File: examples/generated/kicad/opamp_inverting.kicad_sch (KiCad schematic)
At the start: 6 parts

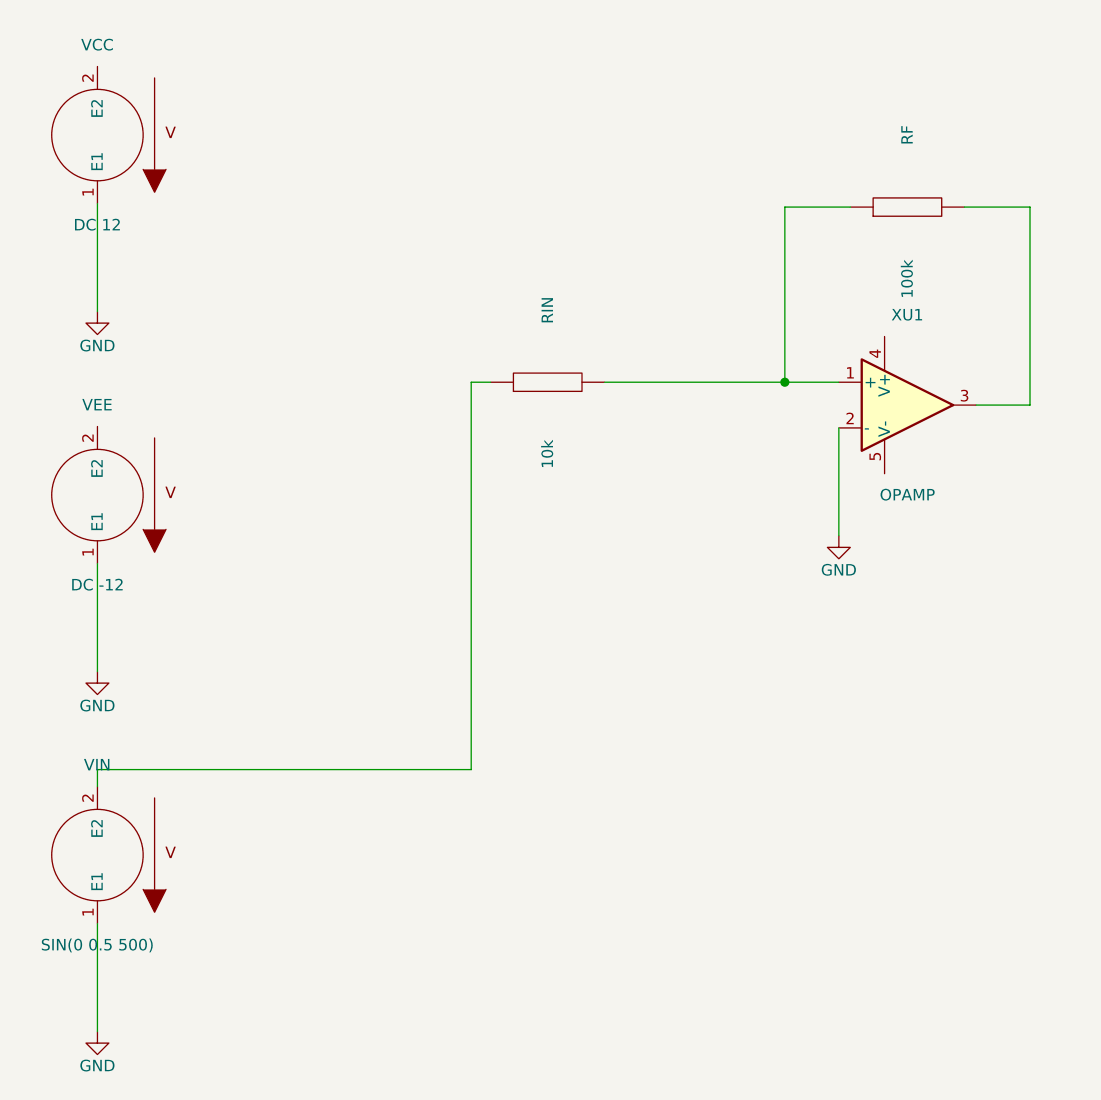
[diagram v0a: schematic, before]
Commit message: Ensure connectivity matches, as measured by opamp connectivity.
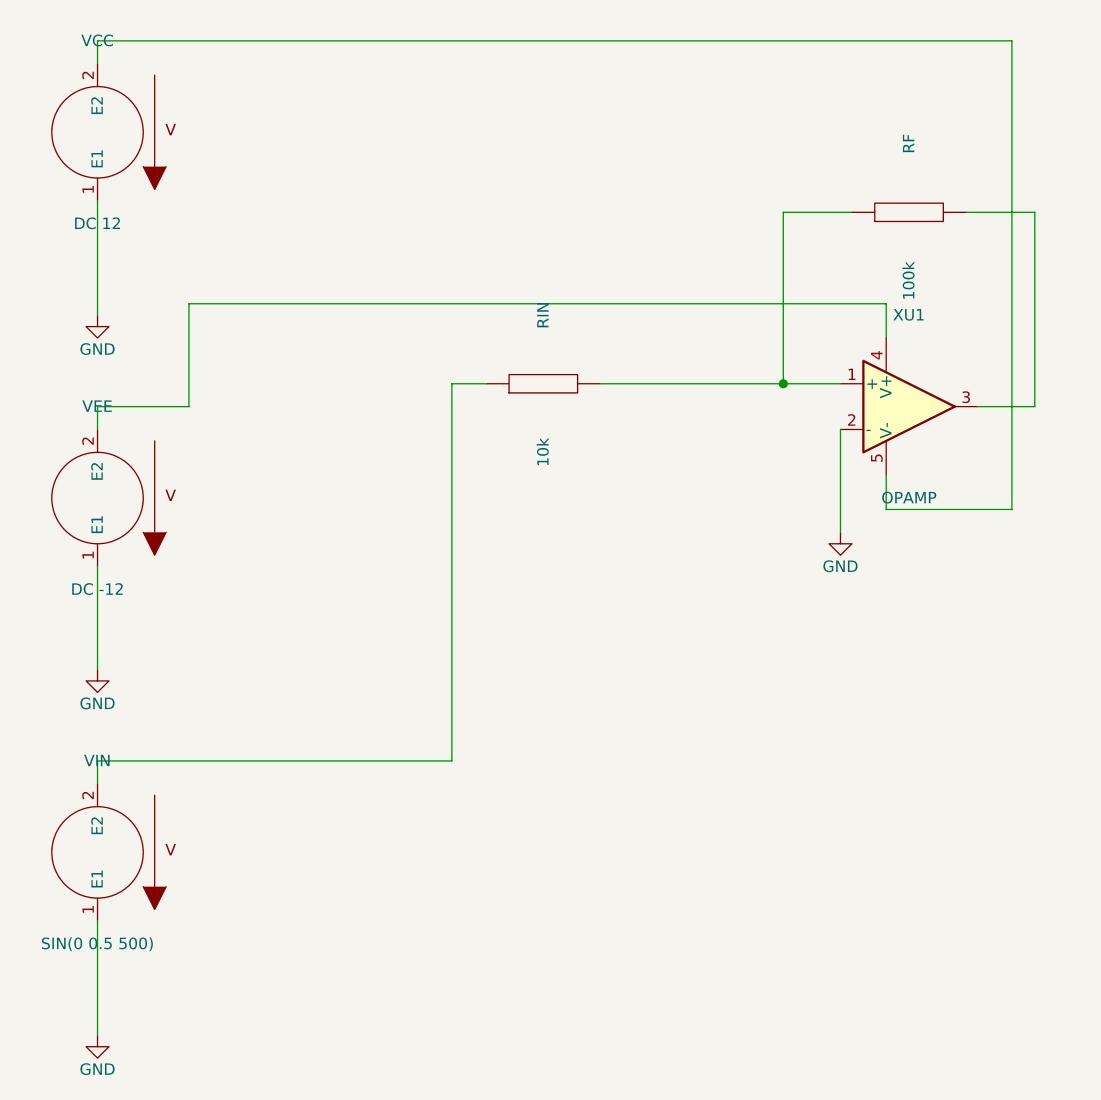
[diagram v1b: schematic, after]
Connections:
- net at VCC.2 (E2): now also XU1.5 (V-)
- net at XU1.4 (V+): now also VEE.2 (E2)
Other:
- moved on the sheet: RF, RIN

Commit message: Refactor further.
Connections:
- net GND: now also XU1.1 (+); no longer XU1.2 (-)
- net vcc: now reaches VCC.2 (E2)
- net vcc: now also XU1.4 (V+); no longer XU1.5 (V-)
- net vminus: now reaches RF.1, RIN.2
- net vminus: now also RF.2, XU1.2 (-), XU1.3; no longer XU1.1 (+)
- net vee: now reaches VEE.2 (E2)
- net vee: now also XU1.5 (V-); no longer XU1.4 (V+)
- net vin: now reaches RIN.1, VIN.2 (E2)
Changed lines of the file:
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@@
     )
+  )
+  (label "vin" (at 123.19 87.63 0)
+    (effects (font (size 1.27 1.27)))
+  )
+  (label "vminus" (at 156.21 92.71 0)
+    (effects (font (size 1.27 1.27)))
+  )
+  (label "vout" (at 184.15 90.17 0)
+    (effects (font (size 1.27 1.27)))
+  )
+  (label "vcc" (at 167.64 82.55 0)
+    (effects (font (size 1.27 1.27)))
+  )
+  (label "vee" (at 167.64 97.79 0)
+    (effects (font (size 1.27 1.27)))
   )
   (wire (pts (xy 80.01 67.31) (xy 80.01 80.01))
@@
     (stroke (width 0) (type solid) (color 0 0 0 0))
   )
-  (wire (pts (xy 162.56 92.71) (xy 162.56 104.14))
+  (wire (pts (xy 162.56 87.63) (xy 162.56 104.14))
     (stroke (width 0) (type solid) (color 0 0 0 0))
   )
@@
     (stroke (width 0) (type solid) (color 0 0 0 0))
   )
-  (wire (pts (xy 162.56 87.63) (xy 156.21 87.63))
+  (wire (pts (xy 156.21 87.63) (xy 156.21 92.71))
     (stroke (width 0) (type solid) (color 0 0 0 0))
   )
-  (wire (pts (xy 163.83 68.58) (xy 156.21 68.58))
+  (wire (pts (xy 162.56 92.71) (xy 156.21 92.71))
     (stroke (width 0) (type solid) (color 0 0 0 0))
   )
-  (wire (pts (xy 156.21 68.58) (xy 156.21 87.63))
+  (wire (pts (xy 176.53 68.58) (xy 180.34 68.58))
+    (stroke (width 0) (type solid) (color 0 0 0 0))
+  )
+  (wire (pts (xy 180.34 68.58) (xy 180.34 49.53))
+    (stroke (width 0) (type solid) (color 0 0 0 0))
+  )
+  (wire (pts (xy 180.34 49.53) (xy 156.21 49.53))
+    (stroke (width 0) (type solid) (color 0 0 0 0))
+  )
+  (wire (pts (xy 156.21 49.53) (xy 156.21 92.71))
     (stroke (width 0) (type solid) (color 0 0 0 0))
   )
@@
     (stroke (width 0) (type solid) (color 0 0 0 0))
   )
-  (wire (pts (xy 176.53 68.58) (xy 184.15 68.58))
+  (wire (pts (xy 163.83 68.58) (xy 160.02 68.58))
     (stroke (width 0) (type solid) (color 0 0 0 0))
   )
-  (wire (pts (xy 184.15 68.58) (xy 184.15 90.17))
+  (wire (pts (xy 160.02 68.58) (xy 160.02 49.53))
     (stroke (width 0) (type solid) (color 0 0 0 0))
   )
-  (wire (pts (xy 167.64 97.79) (xy 167.64 101.60))
+  (wire (pts (xy 160.02 49.53) (xy 184.15 49.53))
     (stroke (width 0) (type solid) (color 0 0 0 0))
   )
-  (wire (pts (xy 167.64 101.60) (xy 181.61 101.60))
-    (stroke (width 0) (type solid) (color 0 0 0 0))
-  )
-  (wire (pts (xy 181.61 101.60) (xy 181.61 49.53))
-    (stroke (width 0) (type solid) (color 0 0 0 0))
-  )
-  (wire (pts (xy 181.61 49.53) (xy 80.01 49.53))
-    (stroke (width 0) (type solid) (color 0 0 0 0))
-  )
-  (wire (pts (xy 80.01 49.53) (xy 80.01 52.07))
+  (wire (pts (xy 184.15 49.53) (xy 184.15 90.17))
     (stroke (width 0) (type solid) (color 0 0 0 0))
   )
@@
     (stroke (width 0) (type solid) (color 0 0 0 0))
   )
-  (wire (pts (xy 90.17 78.74) (xy 90.17 90.17))
+  (wire (pts (xy 90.17 78.74) (xy 90.17 49.53))
     (stroke (width 0) (type solid) (color 0 0 0 0))
   )
-  (wire (pts (xy 90.17 90.17) (xy 80.01 90.17))
+  (wire (pts (xy 90.17 49.53) (xy 80.01 49.53))
+    (stroke (width 0) (type solid) (color 0 0 0 0))
+  )
+  (wire (pts (xy 80.01 49.53) (xy 80.01 52.07))
+    (stroke (width 0) (type solid) (color 0 0 0 0))
+  )
+  (wire (pts (xy 167.64 97.79) (xy 167.64 101.60))
+    (stroke (width 0) (type solid) (color 0 0 0 0))
+  )
+  (wire (pts (xy 167.64 101.60) (xy 80.01 101.60))
+    (stroke (width 0) (type solid) (color 0 0 0 0))
+  )
+  (wire (pts (xy 80.01 101.60) (xy 80.01 90.17))
     (stroke (width 0) (type solid) (color 0 0 0 0))
   )
@@
     (stroke (width 0) (type solid) (color 0 0 0 0))
   )
-  (junction (at 156.21 87.63) (diameter 1.016) (color 0 0 0 0))
+  (junction (at 156.21 92.71) (diameter 1.016) (color 0 0 0 0))
   (sheet_instances
     (path "/" (page "1"))

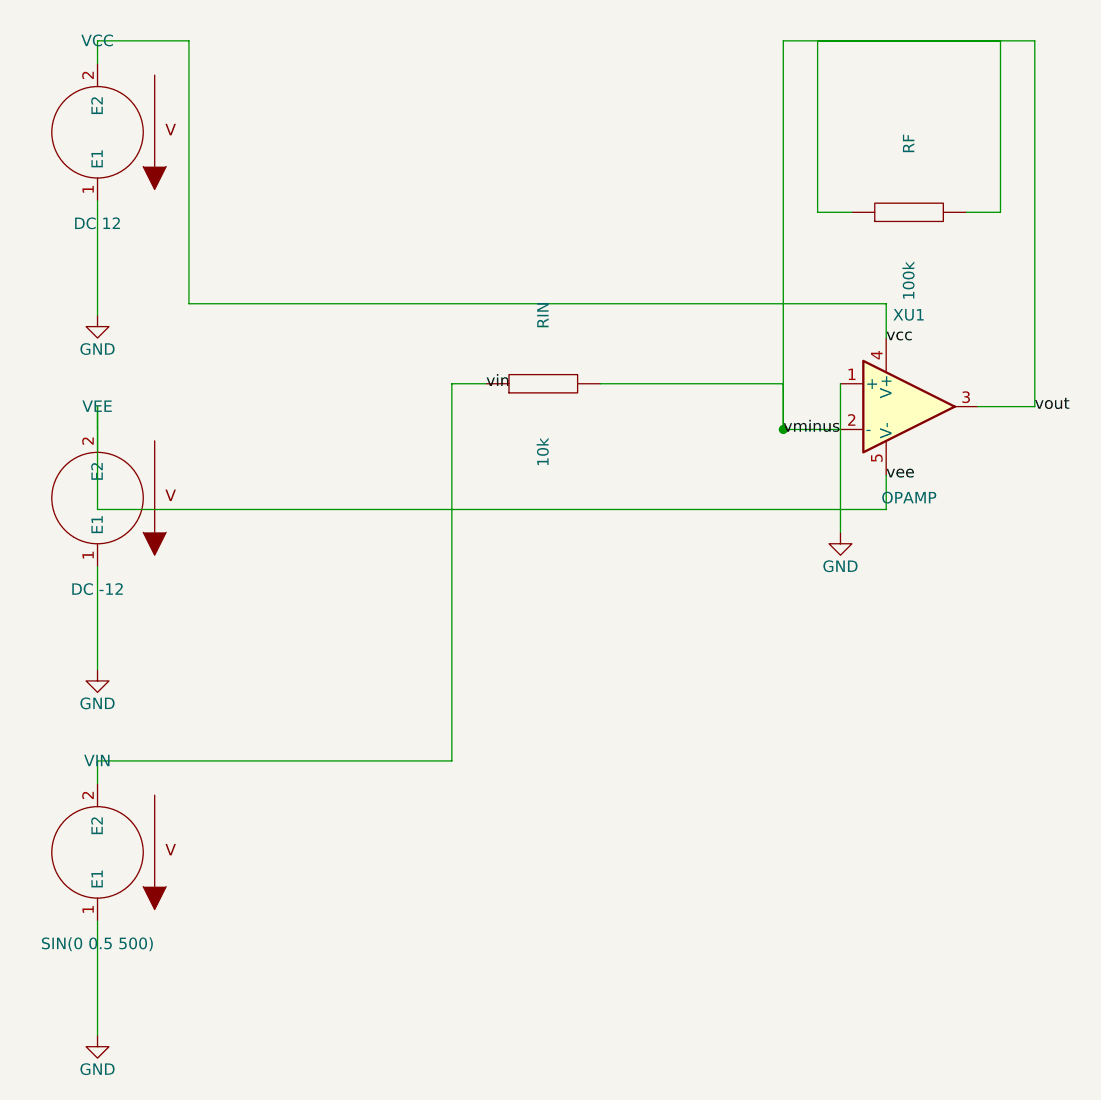
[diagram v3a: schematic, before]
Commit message: Attempt to fix wire kinking (where example showed in cmos inverter).
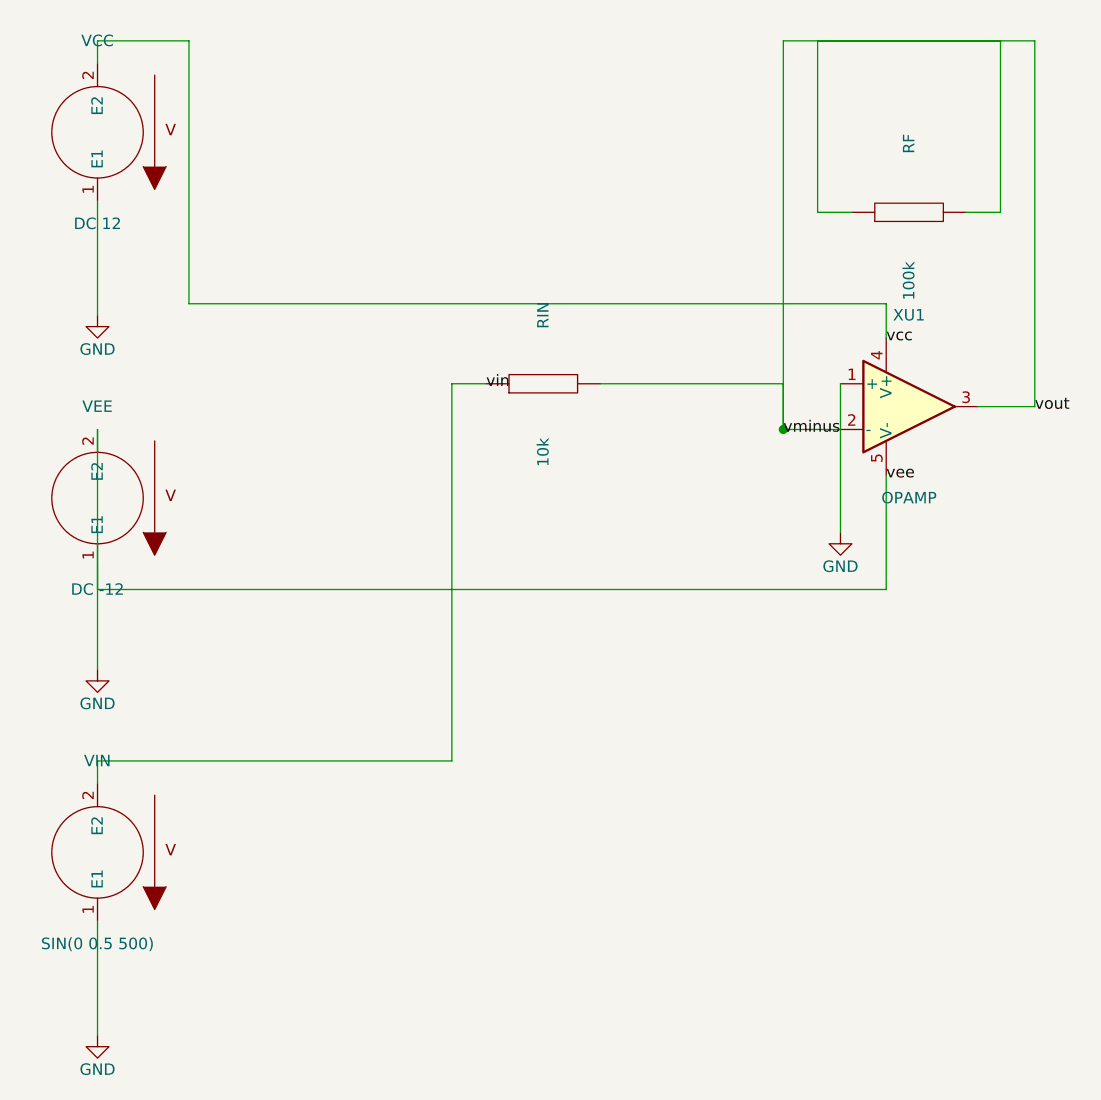
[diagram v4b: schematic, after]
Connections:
- net vee is gone; now on net GND: VEE.2 (E2), XU1.5 (V-)
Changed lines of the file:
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@@
     (stroke (width 0) (type solid) (color 0 0 0 0))
   )
-  (wire (pts (xy 167.64 97.79) (xy 167.64 101.60))
+  (wire (pts (xy 167.64 97.79) (xy 167.64 110.49))
     (stroke (width 0) (type solid) (color 0 0 0 0))
   )
-  (wire (pts (xy 167.64 101.60) (xy 80.01 101.60))
+  (wire (pts (xy 167.64 110.49) (xy 80.01 110.49))
     (stroke (width 0) (type solid) (color 0 0 0 0))
   )
-  (wire (pts (xy 80.01 101.60) (xy 80.01 90.17))
+  (wire (pts (xy 80.01 110.49) (xy 80.01 92.71))
     (stroke (width 0) (type solid) (color 0 0 0 0))
   )
-  (wire (pts (xy 80.01 90.17) (xy 80.01 92.71))
-    (stroke (width 0) (type solid) (color 0 0 0 0))
-  )

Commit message: Attempt to fix inverting op-amp circuit and related issues.
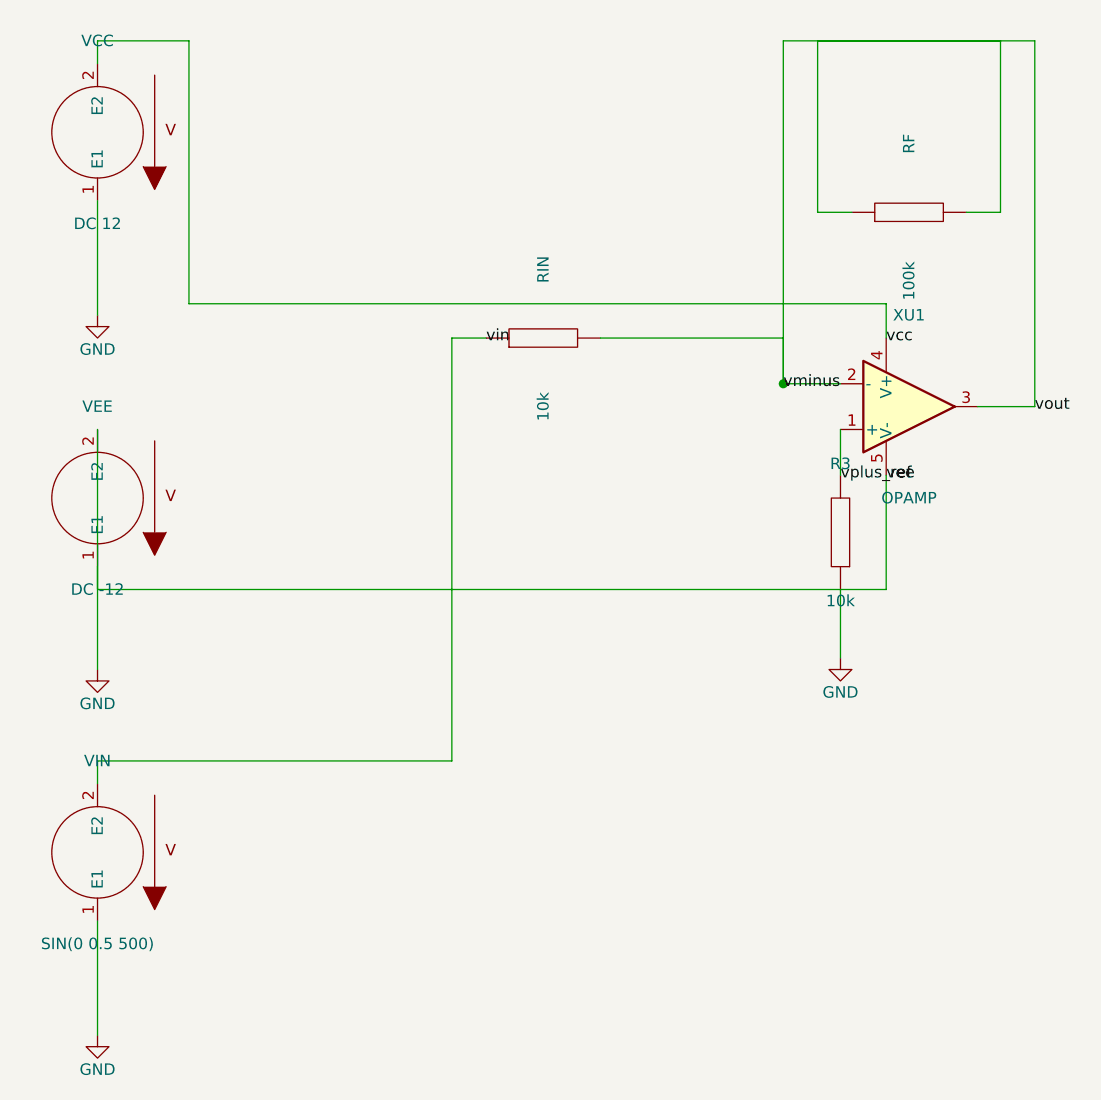
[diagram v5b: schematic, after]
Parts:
- added R3: 10k, symbol R
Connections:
- net GND: now also R3.1; no longer XU1.1 (+)
- new net vplus_ref: R3.2, XU1.1 (+)
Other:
- moved on the sheet: RIN
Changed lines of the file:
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@@
     )
   )
-  (symbol (lib_id "R") (at 129.54 87.63 90) (unit 1)
-    (in_bom yes) (on_board yes)
-    (property "Reference" "RIN" (at 129.54 80.01 0)
-      (effects (font (size 1.27 1.27)))
-    )
-    (property "Value" "10k" (at 129.54 95.25 0)
+  (symbol (lib_id "R") (at 129.54 82.55 90) (unit 1)
+    (in_bom yes) (on_board yes)
+    (property "Reference" "RIN" (at 129.54 74.93 0)
+      (effects (font (size 1.27 1.27)))
+    )
+    (property "Value" "10k" (at 129.54 90.17 0)
       (effects (font (size 1.27 1.27)))
     )
@@
     )
   )
-  (symbol (lib_id "GND") (at 162.56 104.14 0) (unit 1)
-    (in_bom yes) (on_board yes)
-    (property "Reference" "#PWR0001" (at 162.56 100.33 0)
-      (effects (font (size 1.27 1.27)) hide)
-    )
-    (property "Value" "GND" (at 162.56 107.95 0)
+  (symbol (lib_id "R") (at 162.56 104.14 180) (unit 1)
+    (in_bom yes) (on_board yes)
+    (property "Reference" "R3" (at 162.56 96.52 0)
+      (effects (font (size 1.27 1.27)))
+    )
+    (property "Value" "10k" (at 162.56 111.76 0)
+      (effects (font (size 1.27 1.27)))
+    )
+    (property "Footprint" "" (at 0 0 0)
+      (effects (font (size 1.27 1.27)) hide)
+    )
+    (property "Datasheet" "" (at 0 0 0)
+      (effects (font (size 1.27 1.27)) hide)
+    )
+  )
+  (symbol (lib_id "GND") (at 162.56 118.11 0) (unit 1)
+    (in_bom yes) (on_board yes)
+    (property "Reference" "#PWR0001" (at 162.56 114.3 0)
+      (effects (font (size 1.27 1.27)) hide)
+    )
+    (property "Value" "GND" (at 162.56 121.92 0)
       (effects (font (size 1.27 1.27)))
     )
@@
     )
   )
-  (label "vin" (at 123.19 87.63 0)
-    (effects (font (size 1.27 1.27)))
-  )
-  (label "vminus" (at 156.21 92.71 0)
+  (label "vin" (at 123.19 82.55 0)
+    (effects (font (size 1.27 1.27)))
+  )
+  (label "vplus_ref" (at 162.56 97.79 0)
+    (effects (font (size 1.27 1.27)))
+  )
+  (label "vminus" (at 156.21 87.63 0)
     (effects (font (size 1.27 1.27)))
   )
@@
     (stroke (width 0) (type solid) (color 0 0 0 0))
   )
-  (wire (pts (xy 119.38 129.54) (xy 119.38 87.63))
-    (stroke (width 0) (type solid) (color 0 0 0 0))
-  )
-  (wire (pts (xy 119.38 87.63) (xy 123.19 87.63))
-    (stroke (width 0) (type solid) (color 0 0 0 0))
-  )
-  (wire (pts (xy 162.56 87.63) (xy 162.56 104.14))
-    (stroke (width 0) (type solid) (color 0 0 0 0))
-  )
-  (wire (pts (xy 135.89 87.63) (xy 156.21 87.63))
-    (stroke (width 0) (type solid) (color 0 0 0 0))
-  )
-  (wire (pts (xy 156.21 87.63) (xy 156.21 92.71))
-    (stroke (width 0) (type solid) (color 0 0 0 0))
-  )
-  (wire (pts (xy 162.56 92.71) (xy 156.21 92.71))
+  (wire (pts (xy 119.38 129.54) (xy 119.38 82.55))
+    (stroke (width 0) (type solid) (color 0 0 0 0))
+  )
+  (wire (pts (xy 119.38 82.55) (xy 123.19 82.55))
+    (stroke (width 0) (type solid) (color 0 0 0 0))
+  )
+  (wire (pts (xy 162.56 92.71) (xy 162.56 97.79))
+    (stroke (width 0) (type solid) (color 0 0 0 0))
+  )
+  (wire (pts (xy 162.56 110.49) (xy 162.56 118.11))
+    (stroke (width 0) (type solid) (color 0 0 0 0))
+  )
+  (wire (pts (xy 135.89 82.55) (xy 156.21 82.55))
+    (stroke (width 0) (type solid) (color 0 0 0 0))
+  )
+  (wire (pts (xy 156.21 82.55) (xy 156.21 87.63))
+    (stroke (width 0) (type solid) (color 0 0 0 0))
+  )
+  (wire (pts (xy 162.56 87.63) (xy 156.21 87.63))
     (stroke (width 0) (type solid) (color 0 0 0 0))
   )
@@
     (stroke (width 0) (type solid) (color 0 0 0 0))
   )
-  (wire (pts (xy 156.21 49.53) (xy 156.21 92.71))
+  (wire (pts (xy 156.21 49.53) (xy 156.21 87.63))
     (stroke (width 0) (type solid) (color 0 0 0 0))
   )
@@
     (stroke (width 0) (type solid) (color 0 0 0 0))
   )
-  (junction (at 156.21 92.71) (diameter 1.016) (color 0 0 0 0))
+  (junction (at 156.21 87.63) (diameter 1.016) (color 0 0 0 0))
   (sheet_instances
     (path "/" (page "1"))
@@
     (path "/4e95fd71-872b-5cec-ad60-0346b31272ab" (reference "RIN") (unit 1) (value "10k") (footprint ""))
     (path "/2af704cc-8e18-5163-a150-531370848bee" (reference "RF") (unit 1) (value "100k") (footprint ""))
+    (path "/7d3a8dce-1385-5145-b651-aed84918d285" (reference "R3") (unit 1) (value "10k") (footprint ""))
     (path "/2cab4477-b53a-5241-99f6-3f0d34b69ae3" (reference "#PWR0001") (unit 1) (value "GND") (footprint ""))
     (path "/09a203a8-be19-5256-bda7-017ceaed298c" (reference "VCC") (unit 1) (value "DC 12") (footprint ""))
